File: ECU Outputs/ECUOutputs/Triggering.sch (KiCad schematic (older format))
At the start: 28 parts, among them Q2 Q_NPN_BCE, Q3 Q_NPN_BCE, Q4 Q_NPN_BCE, Q5 Q_NPN_BCE

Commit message: Corrected mistake in flip-flop copied from 005 ECU schematic.
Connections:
- net at Q2.2 (C), R15.2: now also R10.1
- net at D4.1 (K), Q2.1 (B), R12.1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: no longer R10.1
- net at Q4.2 (C), R24.2: now also R19.1
- net at D6.1 (K), Q4.1 (B), R21.1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: no longer R19.1
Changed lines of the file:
@@
 Sheet 2 3
 Title "ECU Outputs"
-Date "2021-03-07"
+Date "2021-03-10"
 Rev "1.0"
 Comp "Britishideas.com"
@@
 	4650 2000 4650 2100
 Wire Wire Line
-	4650 2400 4650 2500
+	4650 2400 4650 2450
 Wire Wire Line
 	4650 3300 4650 3200
@@
 Wire Wire Line
 	3050 4200 4350 4200
-Wire Wire Line
-	4350 4200 4350 2700
-Connection ~ 4350 2700
 $Comp
 L Device:R R9
@@
 	9400 2000 9400 2100
 Wire Wire Line
-	9400 2400 9400 2500
+	9400 2400 9400 2450
 Wire Wire Line
 	9400 3300 9400 3200
@@
 Wire Wire Line
 	7800 4200 9100 4200
-Wire Wire Line
-	9100 4200 9100 2700
-Connection ~ 9100 2700
 $Comp
 L Device:R R18
@@
 Wire Wire Line
 	9400 4350 9400 4400
+Wire Wire Line
+	4350 2450 4650 2450
+Connection ~ 4650 2450
+Wire Wire Line
+	4650 2450 4650 2500
+Wire Wire Line
+	4350 2450 4350 4200
+Wire Wire Line
+	9100 2450 9400 2450
+Connection ~ 9400 2450
+Wire Wire Line
+	9400 2450 9400 2500
+Wire Wire Line
+	9100 2450 9100 4200
 $EndSCHEMATC

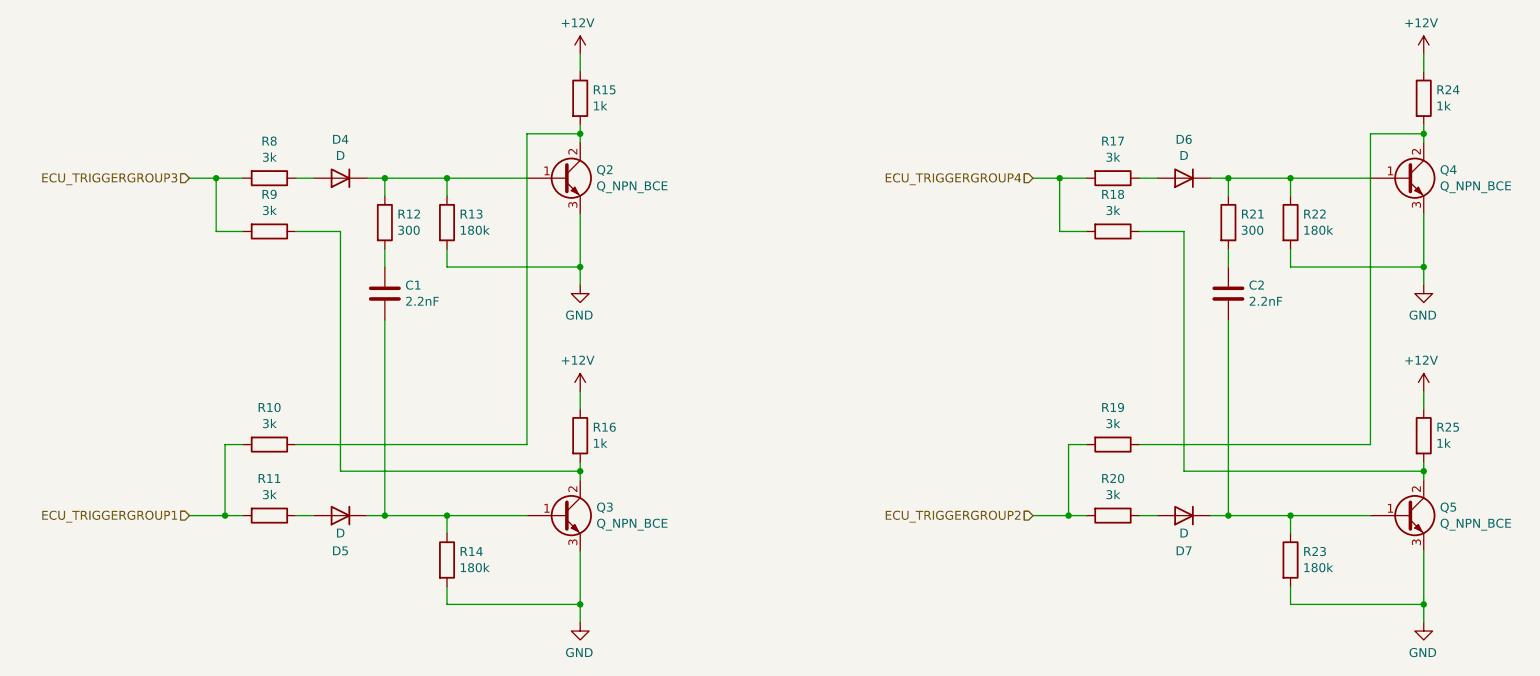
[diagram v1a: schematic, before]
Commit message: Updated manufacturer part numbers. Working on ECU outputs tester board.
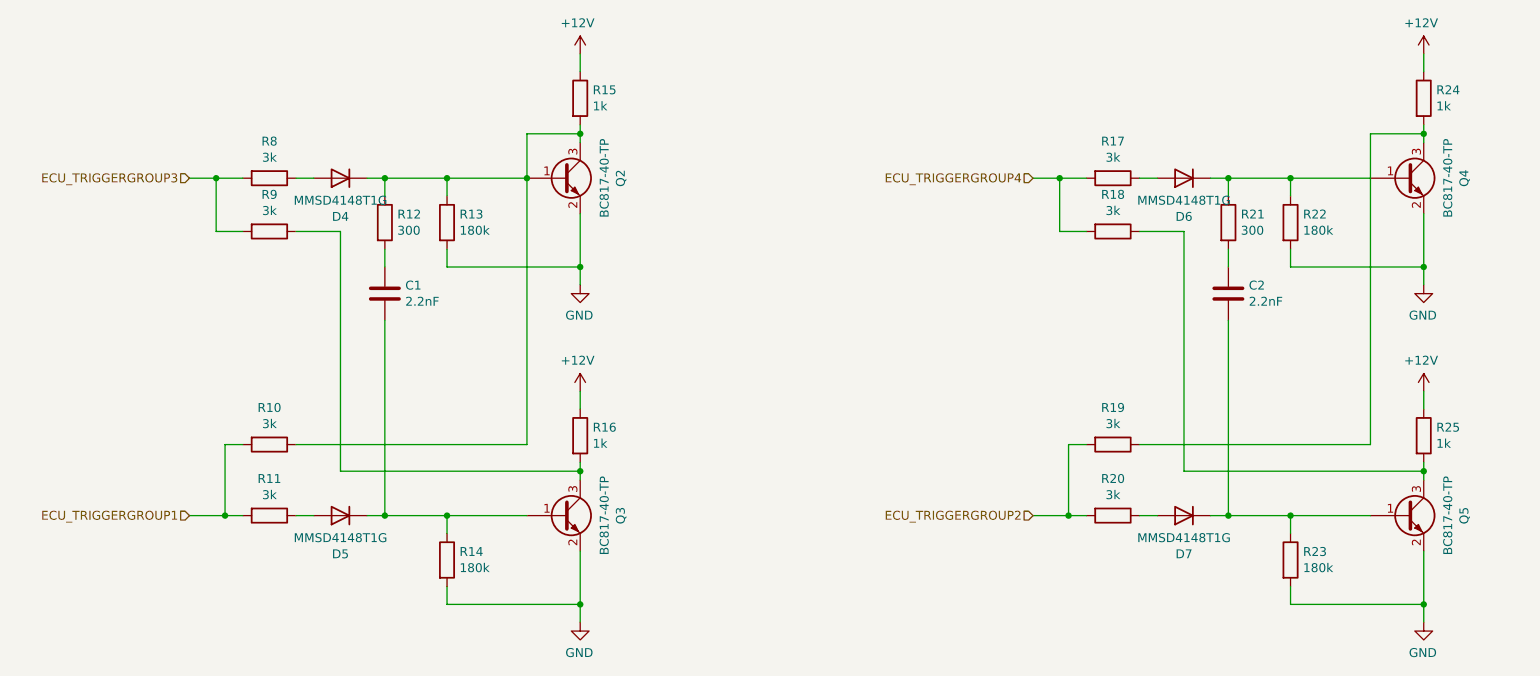
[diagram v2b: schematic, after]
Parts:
- removed Q2, Q3, Q4, Q5: Q_NPN_BCE, symbol Device:Q_NPN_BCE
- added Q2, Q3, Q4, Q5: BC817-40-TP, Package_TO_SOT_SMD:SOT-23, symbol Device:Q_NPN_BEC
- C1, C2: footprint (none) -> Capacitor_SMD:C_0805_2012Metric
- D4, D5, D6, D7: value D -> MMSD4148T1G; footprint (none) -> Diode_SMD:D_SOD-123; manf# (none) -> MMSD4148T1G
- R10, R11, R12, R13, R14, R15, R16, R17, R18, R19, R20, R21, R22, R23, R24, R25, R8, R9: footprint (none) -> Resistor_SMD:R_0805_2012Metric
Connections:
- net GND: now also Q2.2 (E), Q3.2 (E), Q4.2 (E), Q5.2 (E)
- net at R10.1, R15.2: now also D4.1 (K), R12.1, R13.1, Q2.1 (B), Q2.3 (C)
- net at R16.2, R9.1: now also Q3.3 (C)
- net at C1.2, D5.1 (K), R14.1: now also Q3.1 (B)
- net at R19.1, R24.2: now also Q4.3 (C)
- net at D6.1 (K), R21.1, R22.1: now also Q4.1 (B)
- net at R18.1, R25.2: now also Q5.3 (C)
- net at C2.2, D7.1 (K), R23.1: now also Q5.1 (B)
